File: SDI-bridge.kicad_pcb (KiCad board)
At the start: 2 copper layers, 92.7 x 33.8 mm, 94 parts, among them J1 543630489, J2 031-70526-21, J3 3220-10-0100-00, U1 GS2971A, U2 MAX8902B, Y1 ABM7_27.000MH_D2Y_T

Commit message: Initial routing -WIP
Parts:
- added C16: C_33u_0603, antmicro-footprints:0603-cap, F.Cu at (126.0, 102.6)
- C1, C10, C11, C12, C13, C14, C19, C2, C20, C26, C27, C29, C3, C30, C31, C32, C33, C4, C5, C6, C7, C8, C9, R14, R15, R16, R17, R18, R19, R20, R21, R22, R23, R30, R31, R32: moved to B.Cu
- moved C19 107.6 mm to (115.3, 85.0), turned to 0 degrees
- moved C26 105.1 mm to (115.3, 87.1), turned to 0 degrees
- moved C14 103.0 mm to (111.3, 106.0), turned to 90 degrees
- moved R30 102.6 mm to (115.3, 89.1), turned to 180 degrees
- moved C12 101.7 mm to (109.8, 106.0), turned to 90 degrees
- moved C8 101.5 mm to (112.8, 106.0)
- moved C10 100.1 mm to (108.3, 106.0), turned to 90 degrees
- moved R31 100.0 mm to (115.3, 91.1), turned to 180 degrees
- moved C29 97.5 mm to (115.3, 93.1), turned to 0 degrees
- moved C4 97.1 mm to (114.4, 106.0)
- moved C11 96.9 mm to (117.8, 110.5), turned to 90 degrees
- moved C9 95.6 mm to (116.2, 110.5), turned to 90 degrees
- moved C31 95.1 mm to (115.3, 95.1), turned to 0 degrees
- moved C13 94.0 mm to (114.7, 110.5), turned to 90 degrees
- moved C1 93.6 mm to (121.0, 116.5)
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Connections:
- J1 pad 21: /DOUT0 -> /DOUT19
- J1 pad 22: /DOUT1 -> /DOUT18
- J1 pad 23: /DOUT2 -> /DOUT17
- J1 pad 24: /DOUT3 -> /DOUT16
- J1 pad 25: /DOUT4 -> /DOUT15
- J1 pad 26: /DOUT5 -> /DOUT14
- J1 pad 27: /DOUT6 -> /DOUT13
- J1 pad 28: /DOUT7 -> /DOUT12
- J1 pad 29: /DOUT8 -> /DOUT11
- J1 pad 30: /DOUT9 -> /DOUT10
- J1 pad 31: /DOUT10 -> /DOUT9
- J1 pad 32: /DOUT11 -> /DOUT8
- J1 pad 33: /DOUT12 -> /DOUT7
- J1 pad 34: /DOUT13 -> /DOUT6
- J1 pad 35: /DOUT14 -> /DOUT5
- J1 pad 36: /DOUT15 -> /DOUT4
- J1 pad 37: /DOUT16 -> /DOUT3
- J1 pad 38: /DOUT17 -> /DOUT2
- J1 pad 39: /DOUT18 -> /DOUT1
- J1 pad 40: /DOUT19 -> /DOUT0
- R10 pad 1: /D6 -> /DOUT16
- R10 pad 2: /DOUT6 -> /D16
- R11 pad 1: /D7 -> /DOUT17
- R11 pad 2: /DOUT7 -> /D17
- R12 pad 1: /D8 -> /DOUT18
- R12 pad 2: /DOUT8 -> /D18
- R13 pad 1: /D9 -> /DOUT19
- R13 pad 2: /DOUT9 -> /D19
- R14 pad 1: /D10 -> /DOUT9
- R14 pad 2: /DOUT10 -> /D9
- R15 pad 1: /D11 -> /DOUT8
- R15 pad 2: /DOUT11 -> /D8
- R16 pad 1: /D12 -> /DOUT7
- R16 pad 2: /DOUT12 -> /D7
- R17 pad 1: /D13 -> /DOUT6
- R17 pad 2: /DOUT13 -> /D6
- R18 pad 1: /D14 -> /DOUT5
- R18 pad 2: /DOUT14 -> /D5
- R19 pad 1: /D15 -> /DOUT4
- R19 pad 2: /DOUT15 -> /D4
- R20 pad 1: /D16 -> /DOUT3
- R20 pad 2: /DOUT16 -> /D3
- R21 pad 1: /D17 -> /DOUT2
- R21 pad 2: /DOUT17 -> /D2
- R22 pad 1: /D18 -> /DOUT1
- R22 pad 2: /DOUT18 -> /D1
- R23 pad 1: /D19 -> /DOUT0
- R23 pad 2: /DOUT19 -> /D0
- R4 pad 1: /D0 -> /DOUT10
- R4 pad 2: /DOUT0 -> /D10
- R5 pad 1: /D1 -> /DOUT11
- R5 pad 2: /DOUT1 -> /D11
- R6 pad 1: /D2 -> /DOUT12
- R6 pad 2: /DOUT2 -> /D12
- R7 pad 1: /D3 -> /DOUT13
- R7 pad 2: /DOUT3 -> /D13
- R8 pad 1: /D4 -> /DOUT14
- R8 pad 2: /DOUT4 -> /D14
- R9 pad 1: /D5 -> /DOUT15
- R9 pad 2: /DOUT5 -> /D15
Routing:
- net /DATA_ERRORb: track 0.00 -> 61.7 mm, vias 0 -> 3
- net /Y_1ANC: track 0.00 -> 59.6 mm, vias 0 -> 1
- net /LOCKED: track 0.00 -> 54.8 mm, vias 0 -> 1
- net /F_DE: track 0.00 -> 53.9 mm, vias 0 -> 1
- net /~RC_BYP~: track 0.00 -> 50.1 mm, vias 0 -> 1
- net /V_VSYNC: track 0.00 -> 49.2 mm, vias 0 -> 1
- net /H_HSYNC: track 0.00 -> 47.1 mm, vias 0 -> 1
- net /TIM_861: track 0.00 -> 45.4 mm, vias 0 -> 1
- net /~SMPTE_BYPASS~: track 0.00 -> 44.7 mm, vias 0 -> 1
- net /PCLK: track 0.00 -> 43.0 mm, vias 0 -> 1
- net /20bit_~10bit~: track 0.00 -> 42.1 mm, vias 0 -> 1
- net /DVB_ASI: track 0.00 -> 40.9 mm, vias 0 -> 3
- net GNDREF: track 0.00 -> 28.9 mm, vias 0 -> 11
- net GNDA: track 0.00 -> 20.5 mm, vias 0 -> 6
- net /D19: track 0.00 -> 18.0 mm
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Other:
- board size 92.7 x 33.8 mm -> 60 x 30 mm
- net class Default: clearance 0.2 -> 0.15; trace_width 0.25 -> 0.15; via_dia 0.8 -> 0.55; via_drill 0.4 -> 0.15
- rule trace_clearance: 0.2 -> 0.15
- rule trace_min: 0.2 -> 0.15
- rule via_min_drill: 0.3 -> 0.15
- rule via_min_size: 0.4 -> 0.55

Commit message: Add routing - WIP
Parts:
- added R42: R_0R_0402, antmicro-footprints:0402-res, B.Cu at (131.3, 110.5)
- C19, C20, C26, C27, C29, C30, C31, C32, R30, R31, R32: moved to F.Cu
- moved TP1 61.9 mm to (120.5, 102.0)
- moved C19 48.9 mm to (151.5, 117.9), turned to 90 degrees
- moved C26 46.4 mm to (149.9, 117.9), turned to 90 degrees
- moved R30 41.5 mm to (148.9, 113.4)
- moved R31 41.4 mm to (148.9, 115.4)
- moved C29 41.3 mm to (148.3, 117.9), turned to 90 degrees
- moved C31 38.8 mm to (146.7, 117.9), turned to 90 degrees
- moved C32 34.6 mm to (148.3, 109.1), turned to 90 degrees
- moved C27 33.5 mm to (151.5, 109.1), turned to 90 degrees
- moved C30 31.5 mm to (146.7, 109.1), turned to 90 degrees
- moved C20 30.7 mm to (149.9, 109.1), turned to 90 degrees
- moved R32 26.5 mm to (148.9, 111.4), turned to 180 degrees
- moved TP4 23.9 mm to (153.0, 113.2)
- moved TP2 22.4 mm to (156.2, 121.4)
- moved C33 21.8 mm to (129.9, 110.5), turned to 90 degrees
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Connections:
- C2 pad 1: +3V3 -> +VSW
- C33 pad 1: +3V3 -> +VSW
- C4 pad 1: +3V3 -> +VSW
- C6 pad 1: +3V3 -> +VSW
- C8 pad 1: +3V3 -> +VSW
- U1 pad A7: +3V3 -> +VSW
- U1 pad D10: +3V3 -> +VSW
- U1 pad G10: +3V3 -> +VSW
- U1 pad K7: +3V3 -> +VSW
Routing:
- net GNDA: track 20.5 -> 54.1 mm, vias 6 -> 29
- net +VSW: track 0.00 -> 29.7 mm, vias 0 -> 10
- net /SDIN_TDI: track 9.91 -> 39.4 mm, vias 1 -> 2
- net /SDOUT_TDO: track 8.91 -> 34.2 mm
- net /~CS~_TMS: track 8.91 -> 32.2 mm, vias 1 -> 2
- net /SCLK_TCK: track 9.91 -> 27.5 mm
- net Net-(C15-Pad2): track 0.00 -> 17.2 mm
- net GNDREF: track 28.9 -> 46.0 mm, vias 11 -> 27
- net +3.3VA: track 4.50 -> 21.2 mm, vias 0 -> 5
- net VPP: track 4.12 -> 19.7 mm, vias 2 -> 6
- net +1V2: track 7.33 -> 18.2 mm, vias 4 -> 11
- net Net-(R1-Pad2): track 1.50 -> 10.1 mm
- net Net-(R2-Pad2): track 2.71 -> 11.2 mm
- net Net-(R3-Pad2): track 4.12 -> 11.7 mm, vias 1 -> 2
- net +3V3: track 12.7 -> 5.46 mm, vias 7 -> 3
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- added copper zone on In1.Cu, net +1V2
- added copper zone on In1.Cu, net +3.3VA
- added copper zone on In1.Cu, net +VSW
- added copper zone on In2.Cu, net GNDA
- added copper zone on In2.Cu, net GNDREF
- added copper zone on In1.Cu, net VPP
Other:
- copper layers 2 -> 4
- net class Power_supply added: clearance 0.15, trace_width 0.2, via_dia 0.55, via_drill 0.15

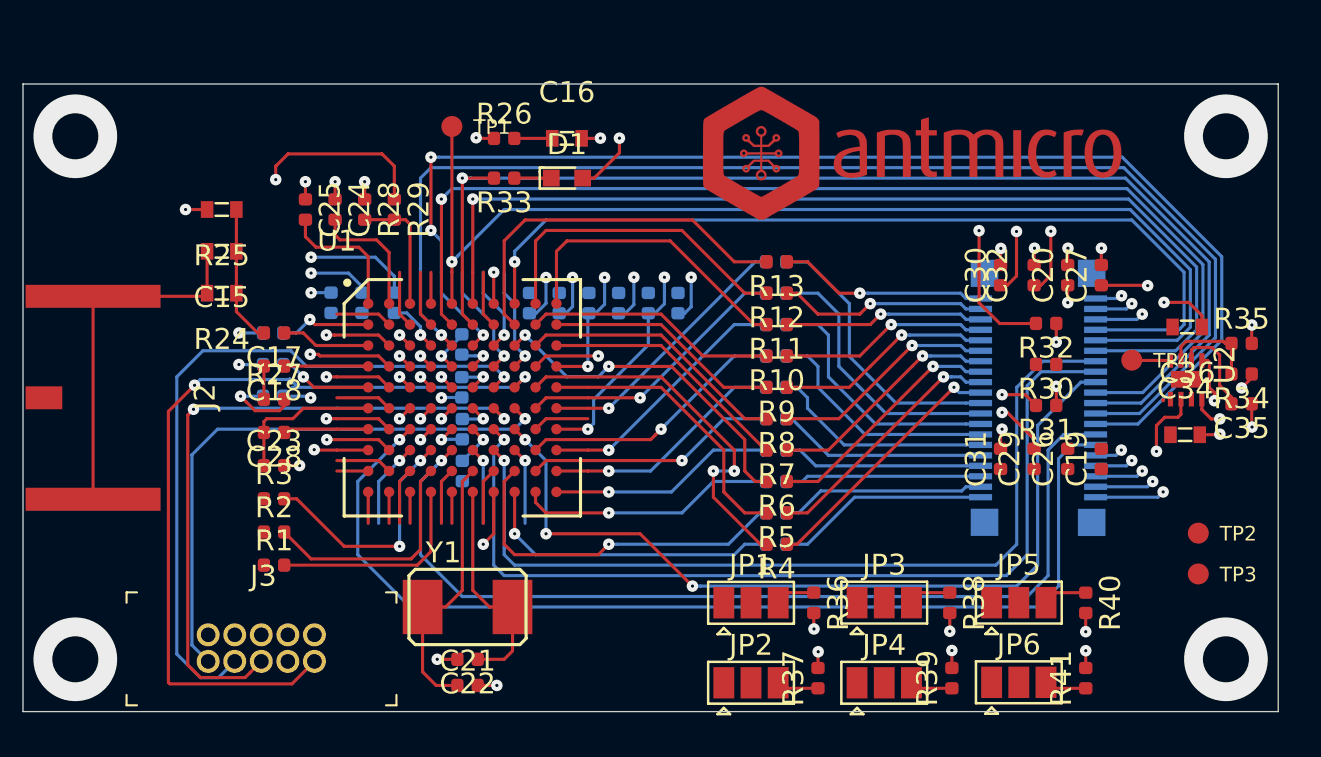
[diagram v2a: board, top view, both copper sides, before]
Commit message: Add complete routing
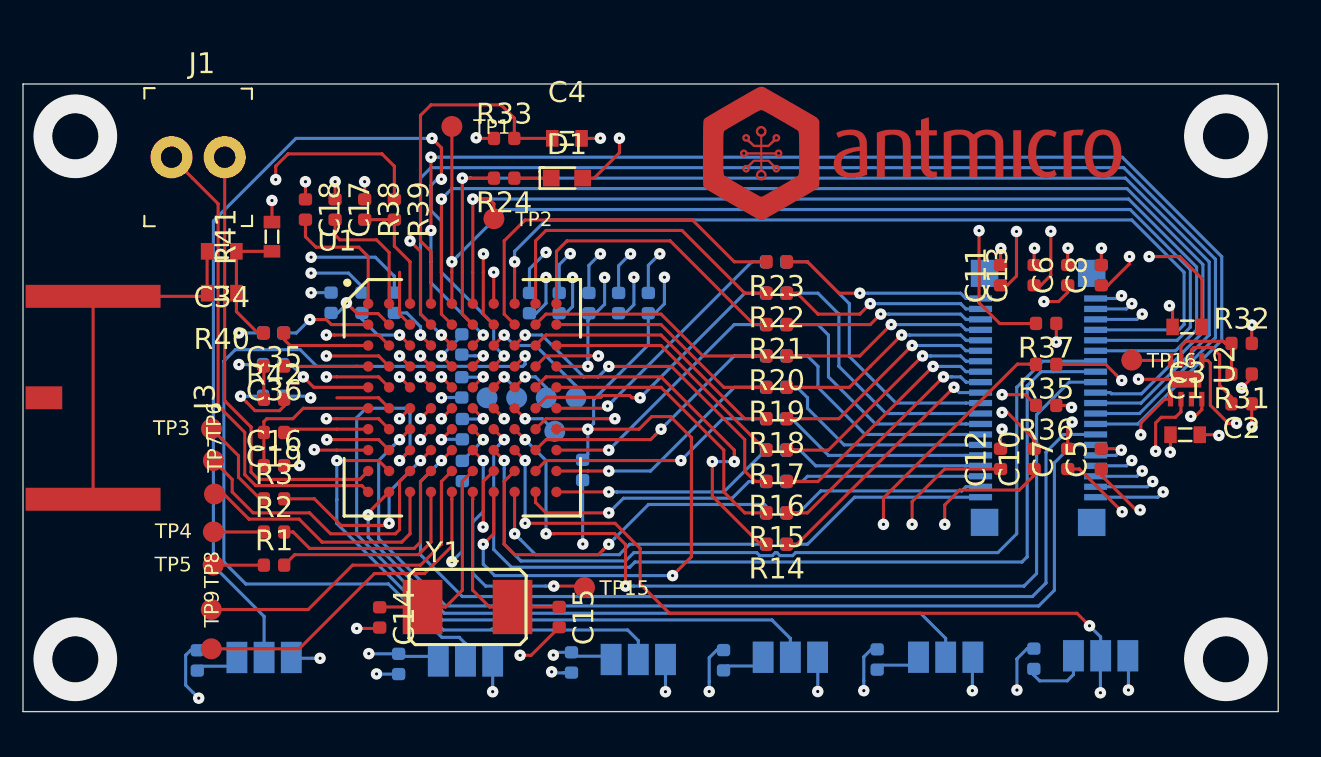
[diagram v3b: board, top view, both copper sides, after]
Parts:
- removed the J3 at (108.8, 127.6)
- removed the R36 at (137.8, 124.8)
- removed the R37 at (138.0, 128.4)
- removed the R38 at (144.3, 124.8)
- removed the R39 at (144.4, 128.4)
- removed the R40 at (150.8, 124.8)
- removed the R41 at (150.8, 128.4)
- removed the R42 at (131.3, 110.5)
- added J1: 22-23-2021, antmicro-footprints:PinHeader_1x2_P2.54mm_Drill1.02mm, F.Cu at (107.1, 103.5)
- added R25: R_0R_0402, antmicro-footprints:0402-res, B.Cu at (118.0, 127.7)
- added R26: R_0R_0402, antmicro-footprints:0402-res, B.Cu at (133.5, 127.5)
- added R27: R_0R_0402, antmicro-footprints:0402-res, B.Cu at (126.2, 127.7)
- added R28: R_0R_0402, antmicro-footprints:0402-res, B.Cu at (148.3, 127.5)
- added R29: R_0R_0402, antmicro-footprints:0402-res, B.Cu at (140.8, 127.5)
- added R30: R_0R_0402, antmicro-footprints:0402-res, B.Cu at (108.3, 127.6)
- added R34: R_0R_0402, antmicro-footprints:0402-res, B.Cu at (126.8, 118.5)
- added TP10: TP_SMD1MM, antmicro-footprints:Testpoint_smd_1mm, B.Cu at (125.4, 116.7)
- added TP11: TP_SMD1MM, antmicro-footprints:Testpoint_smd_1mm, B.Cu at (123.6, 115.1)
- added TP12: TP_SMD1MM, antmicro-footprints:Testpoint_smd_1mm, B.Cu at (122.2, 115.0)
- added TP13: TP_SMD1MM, antmicro-footprints:Testpoint_smd_1mm, B.Cu at (125.0, 115.1)
- added TP14: TP_SMD1MM, antmicro-footprints:Testpoint_smd_1mm, B.Cu at (126.4, 115.1)
- added TP3: TP_SMD1MM, antmicro-footprints:Testpoint_smd_1mm, F.Cu at (109.0, 116.5)
- added TP4: TP_SMD1MM, antmicro-footprints:Testpoint_smd_1mm, F.Cu at (109.1, 121.5)
- added TP5: TP_SMD1MM, antmicro-footprints:Testpoint_smd_1mm, F.Cu at (109.1, 123.1)
- added TP6: TP_SMD1MM, antmicro-footprints:Testpoint_smd_1mm, F.Cu at (109.0, 118.0)
- added TP7: TP_SMD1MM, antmicro-footprints:Testpoint_smd_1mm, F.Cu at (109.1, 119.6)
- added TP8: TP_SMD1MM, antmicro-footprints:Testpoint_smd_1mm, F.Cu at (108.9, 125.1)
- added TP9: TP_SMD1MM, antmicro-footprints:Testpoint_smd_1mm, F.Cu at (108.9, 127.0)
- JP1, JP2, JP3, JP4, JP5, JP6: moved to B.Cu
- moved TP2 36.9 mm to (122.5, 106.4)
- moved JP6 36.1 mm to (111.5, 127.4), turned to 180 degrees
- moved TP15 29.3 mm to (126.8, 124.0)
- moved JP1 13.9 mm to (121.2, 127.6), turned to 180 degrees
- moved JP3 12.1 mm to (129.4, 127.5), turned to 180 degrees
- moved JP4 10.4 mm to (151.5, 127.3), turned to 180 degrees
- moved C14 5.31 mm to (117.0, 125.5), turned to 270 degrees
- moved C15 4.82 mm to (125.6, 125.5), turned to 270 degrees
- moved JP5 4.36 mm to (144.1, 127.4), turned to 180 degrees
- moved R41 2.73 mm to (111.9, 107.3), turned to 90 degrees
- moved JP2 2.24 mm to (136.7, 127.4), turned to 180 degrees
- renumbered C34 to C1, C29 to C10, C30 to C11, C31 to C12, C32 to C13, C21 to C14, C22 to C15, C23 to C16, C24 to C17, C25 to C18, C28 to C19, C35 to C2, C1 to C20, C2 to C21, C3 to C22, C4 to C23, C5 to C24, C6 to C25, C7 to C26, C8 to C27, C9 to C28, C10 to C29, C36 to C3, C11 to C30, C12 to C31, C13 to C32, C14 to C33, C15 to C34, C17 to C35, C18 to C36, C16 to C4, C19 to C5, C20 to C6, C26 to C7, C27 to C8, C33 to C9, J1 to J2, J2 to J3, R17 to R10, R16 to R11, R15 to R12, R14 to R13, R4 to R14, R5 to R15, R6 to R16, R7 to R17, R8 to R18, R9 to R19, R10 to R20, R11 to R21, R12 to R22, R13 to R23, R33 to R24, R34 to R31, R35 to R32, R26 to R33, R30 to R35, R31 to R36, R32 to R37, R28 to R38, R29 to R39, R23 to R4, R24 to R40, R25 to R41, R27 to R42, R22 to R5, R21 to R6, R20 to R7, R19 to R8, R18 to R9, TP3 to TP15, TP4 to TP16
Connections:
- C3 pad 2: Net-(C36-Pad2) (its old number) -> GNDREF
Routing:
- net /SW_EN: track 5.54 -> 47.0 mm, vias 1 -> 3
- net /SDIN_TDI: track 39.4 -> 2.42 mm, vias 2 -> 1
- net /JTAG_~HOST~: track 5.12 -> 39.8 mm
- net /IOPROC_EN_~DIS~: track 3.71 -> 37.1 mm, vias 1 -> 4
- net /SDOUT_TDO: track 34.2 -> 1.95 mm
- net /STANDBY: track 1.50 -> 33.1 mm, vias 0 -> 1
- net /Audio_EN_~DIS~: track 4.12 -> 35.3 mm
- net GNDREF: track 46.0 -> 77.1 mm, vias 27 -> 39
- net /~CS~_TMS: track 32.2 -> 2.05 mm, vias 2 -> 1
- net +3V3: track 5.46 -> 30.7 mm, vias 3 -> 15
- net /SCLK_TCK: track 27.5 -> 2.38 mm
- net +3.3VA: track 21.2 -> 44.5 mm, vias 5 -> 8
- net +VSW: track 29.7 -> 51.9 mm
- net /~SDO~: track 1.50 -> 22.9 mm
- net /SDO_EN_DIS: track 2.71 -> 23.4 mm, vias 0 -> 1
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- added copper zone on In1.Cu, net +3V3

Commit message: Clean Designators
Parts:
- moved N1 1.83 mm to (140.7, 103.7)
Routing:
- net VPP: track 22.8 -> 22.2 mm
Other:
- board text added: "JTAG"
- board text added: "Rev.1.0 02/2020"
- board text added: "SDI Bridge"
